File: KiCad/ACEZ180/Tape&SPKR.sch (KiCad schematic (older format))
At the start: 27 parts, among them Q3 BC237

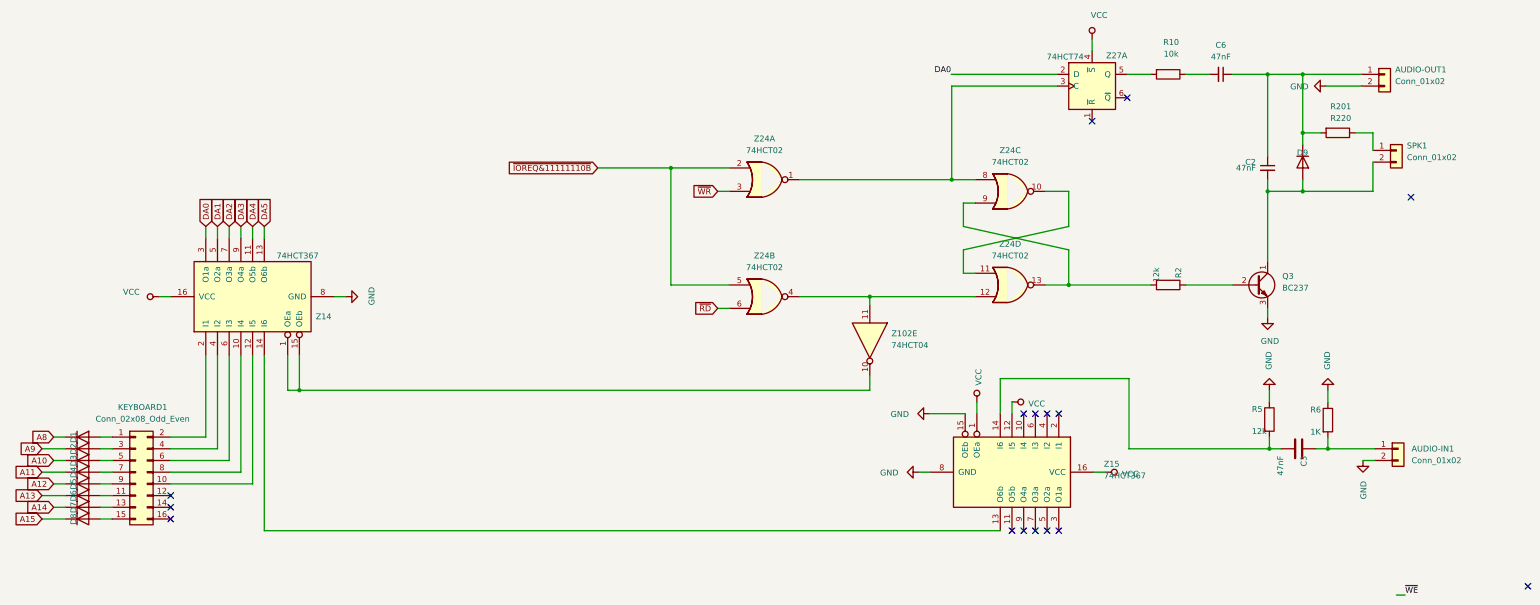
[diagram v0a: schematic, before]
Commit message: Add Extra IO to Z180 board.
Signed-off-by: John Bradley <flypie@rocketmail.com>
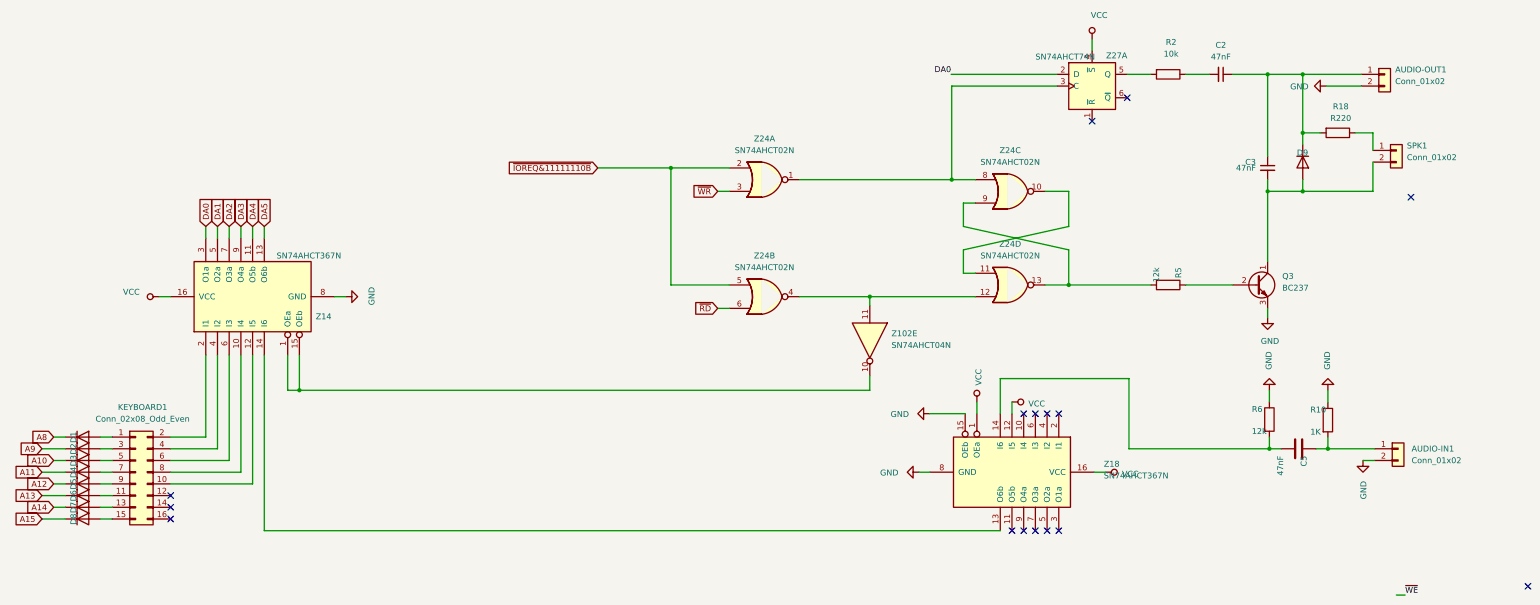
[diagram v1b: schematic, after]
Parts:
- Z102: value 74HCT04 -> SN74AHCT04N
- Z14: value 74HCT367 -> SN74AHCT367N
- Z18: renamed from Z15; value 74HCT367 -> SN74AHCT367N
- Z24: value 74HCT02 -> SN74AHCT02N
- Z27: value 74HCT74 -> SN74AHCT74N
- renumbered C6 to C2, C2 to C3, C3 to C5, R6 to R10, R201 to R18, R10 to R2, R2 to R5, R5 to R6

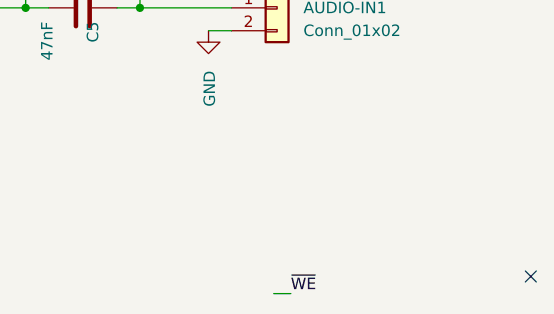
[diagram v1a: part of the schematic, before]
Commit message: Move Towards Ac3 test board, include KIO chip, regaranged port selection, ROM exapsion to 3000-3FFF relocated base of RAM to 4000 and inrease RAM to 48k. Change 40Hz interupt to work via CLK/TRG3 so the IM can be changed to use IM 2. This will require updated ROM.
Signed-off-by: John Bradley <flypie@rocketmail.com>
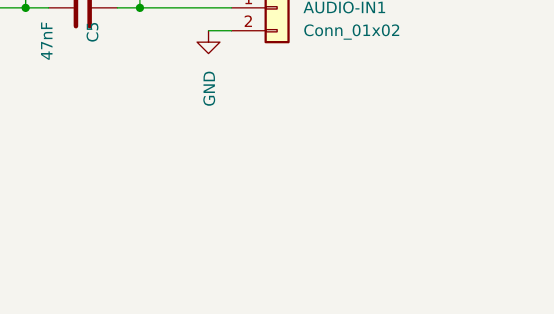
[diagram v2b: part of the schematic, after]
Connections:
- no-connect marks 16 -> 15
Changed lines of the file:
@@
 NoConn ~ 11375 3300
 NoConn ~ 11075 3500
-Wire Wire Line
-	13675 7550 13750 7550
-Text Label 13750 7550 0    50   ~ 0
-~WE
-NoConn ~ 14800 7475
 $Comp
 L Connector_Generic:Conn_01x02 SPK1

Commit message: Tidy up Capcitors in power supply to remove errors add labels.
Primary Development is now ACE3NOKB.


Signed-off-by: John Bradley <flypie@rocketmail.com>
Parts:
- C2, C3, C5: footprint Capacitor_THT:C_Disc_D5.0mm_W2.5mm_P5.00mm -> Capacitor_THT:C_Disc_D3.0mm_W1.6mm_P2.50mm
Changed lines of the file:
@@
 EESchema Schematic File Version 4
-LIBS:acez180-cache
-EELAYER 29 0
+EELAYER 30 0
 EELAYER END
 $Descr A3 16535 11693
@@
 F 0 "C5" H 12900 6315 50  0000 L BNN
 F 1 "47nF" H 12900 6115 50  0000 L BNN
-F 2 "Capacitor_THT:C_Disc_D5.0mm_W2.5mm_P5.00mm" H 12840 6300 50  0001 C CNN
+F 2 "Capacitor_THT:C_Disc_D3.0mm_W1.6mm_P2.50mm" H 12840 6300 50  0001 C CNN
 F 3 "~" H 12840 6300 50  0001 C CNN
 	1    12840 6300
@@
 F 0 "C2" V 11925 3100 50  0000 C CNN
 F 1 "47nF" V 12025 3100 50  0000 C CNN
-F 2 "Capacitor_THT:C_Disc_D5.0mm_W2.5mm_P5.00mm" H 12175 3100 50  0001 C CNN
+F 2 "Capacitor_THT:C_Disc_D3.0mm_W1.6mm_P2.50mm" H 12175 3100 50  0001 C CNN
 F 3 "~" H 12175 3100 50  0001 C CNN
 	1    12175 3100
@@
 F 0 "C3" H 12475 3950 50  0000 R CNN
 F 1 "47nF" H 12475 3900 50  0000 R CNN
-F 2 "Capacitor_THT:C_Disc_D5.0mm_W2.5mm_P5.00mm" H 12575 3900 50  0001 C CNN
+F 2 "Capacitor_THT:C_Disc_D3.0mm_W1.6mm_P2.50mm" H 12575 3900 50  0001 C CNN
 F 3 "~" H 12575 3900 50  0001 C CNN
 	1    12575 3900
@@
 U 1 1 5F80CB50
 P 11075 3200
+AR Path="/5F80CB50" Ref="Z27"  Part="1"
+AR Path="/5D66C06C/5F80CB50" Ref="Z27"  Part="1"
 F 0 "Z27" H 11285 3460 50  0000 C CNN
 F 1 "SN74AHCT74N" H 10845 3450 50  0000 C CNN

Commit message: Double check transistors
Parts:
- Q3: value BC237 -> BC183; symbol Transistor_BJT:BC237 -> Device:Q_NPN_CBE
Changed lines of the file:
@@
 	9875 3200 9875 4000
 $Comp
-L Transistor_BJT:BC237 Q3
+L Device:Q_NPN_CBE Q3
 U 1 1 5F80CB45
 P 12475 4900
 F 0 "Q3" H 12700 4975 50  0000 L CNN
-F 1 "BC237" H 12700 4875 50  0000 L CNN
+F 1 "BC183" H 12700 4875 50  0000 L CNN
 F 2 "Package_TO_SOT_THT:TO-92_Inline" H 12675 4825 50  0001 L CIN
-F 3 "http:~/www.onsemi.com/pub_link/Collateral/BC237-D.PDF" H 12475 4900 50  0001 L CNN
+F 3 "Package_TO_SOT_THT:TO-18-3" H 12475 4900 50  0001 L CNN
 	1    12475 4900
 	1    0    0    -1
